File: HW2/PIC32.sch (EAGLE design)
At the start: 12 parts

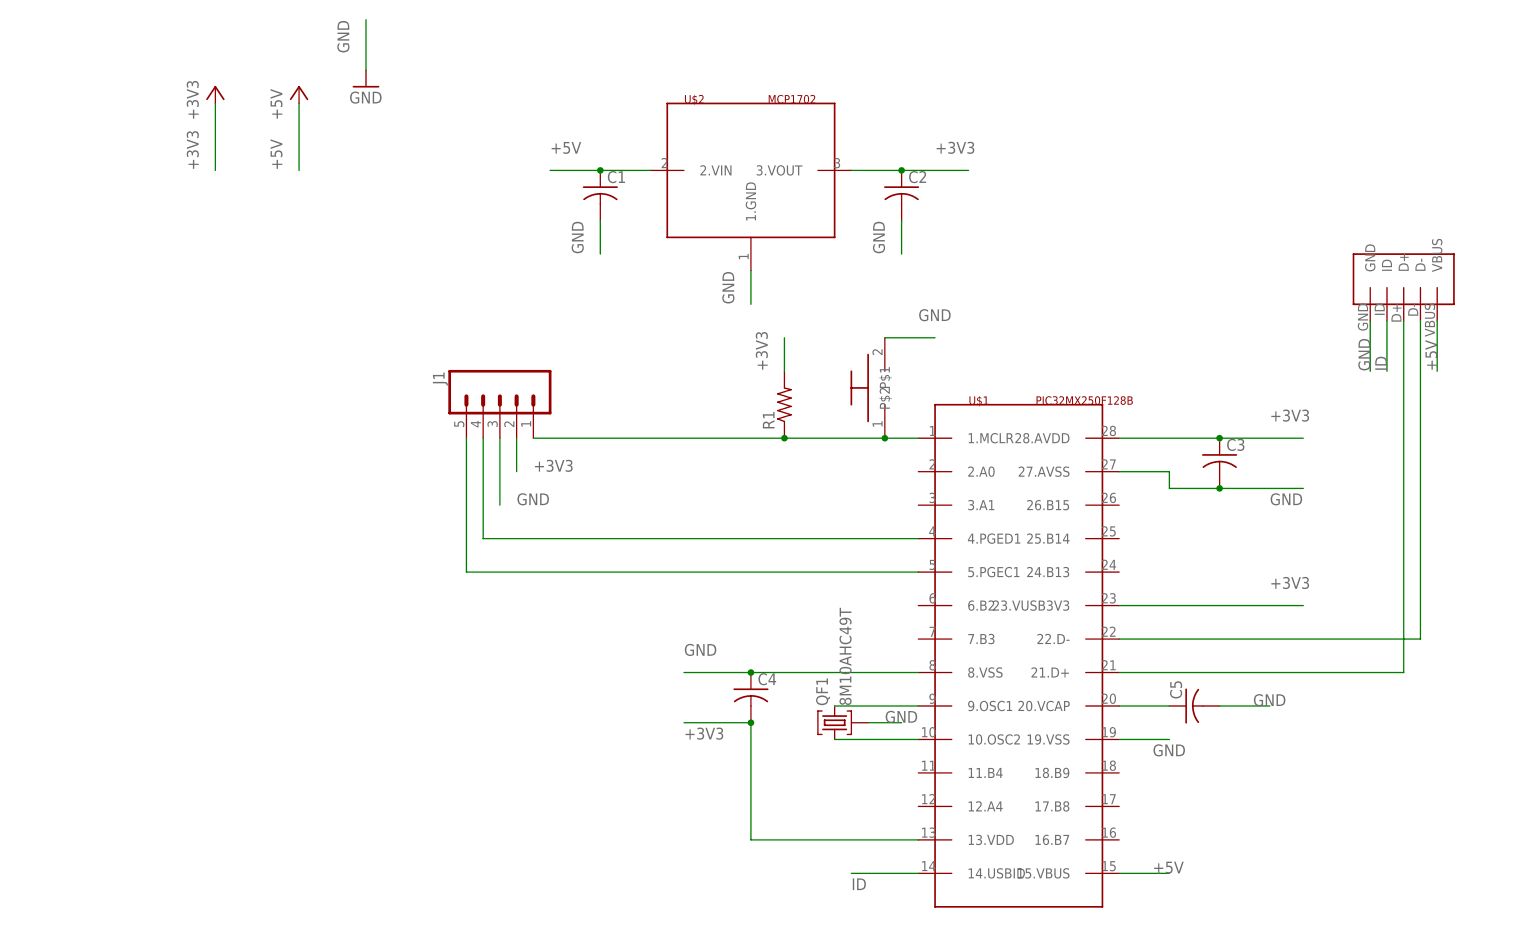
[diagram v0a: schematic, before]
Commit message: Added header pins
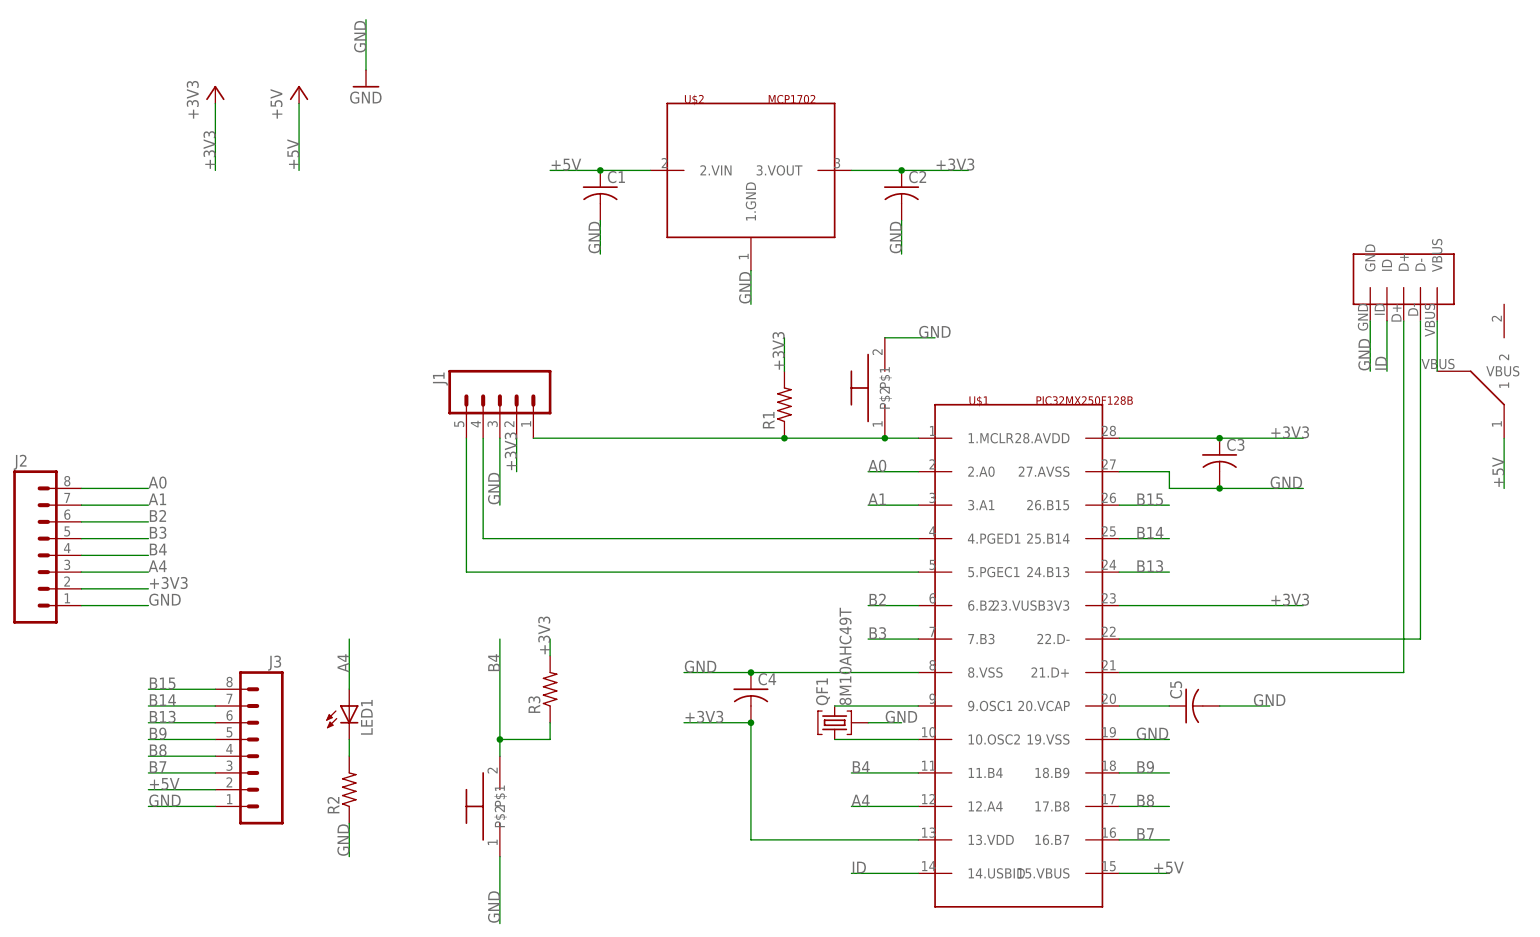
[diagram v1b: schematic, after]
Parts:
- added J2, J3: (no value), ME433:M08
- added LED1: (no value), led:LED3MM
- added R2, R3: (no value), ME433:R-US_0207/10
- added U$5: PUSHBUTTON, ME433:PUSHBUTTON
- added U$6: SLIDESWITCH, ME433:SLIDESWITCH
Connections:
- new net A0: J2.8, U$1.2.A0
- new net A1: J2.7, U$1.3.A1
- new net A4: J2.3, LED1.A, U$1.12.A4
- new net B13: J3.6, U$1.24.B13
- new net B14: J3.7, U$1.25.B14
- new net B15: J3.8, U$1.26.B15
- new net B2: J2.6, U$1.6.B2
- new net B3: J2.5, U$1.7.B3
- new net B4: J2.4, R3.1, U$1.11.B4, U$5.P$2
- new net B7: J3.3, U$1.16.B7
- new net B8: J3.4, U$1.17.B8
- new net B9: J3.5, U$1.18.B9
- new net N$6: LED1.C, R2.2
- new net N$7: U$4.VBUS, U$6.VBUS
- net +3V3: now also J2.2, R3.2
- net +5V: now also J3.2, U$6.1; no longer U$4.VBUS
- net GND: now also J2.1, J3.1, R2.1, U$5.P$1
